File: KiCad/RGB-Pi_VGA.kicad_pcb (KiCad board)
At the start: 2 copper layers, 85 x 43.6 mm, 39 parts, among them J1 Raspberry_Pi_4, J2 SCART-F, J3 DE15_Plug_HighDensity_Mountin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, J4 SJ1-3535NG, Q1 MMBT3904, U1 ST662A

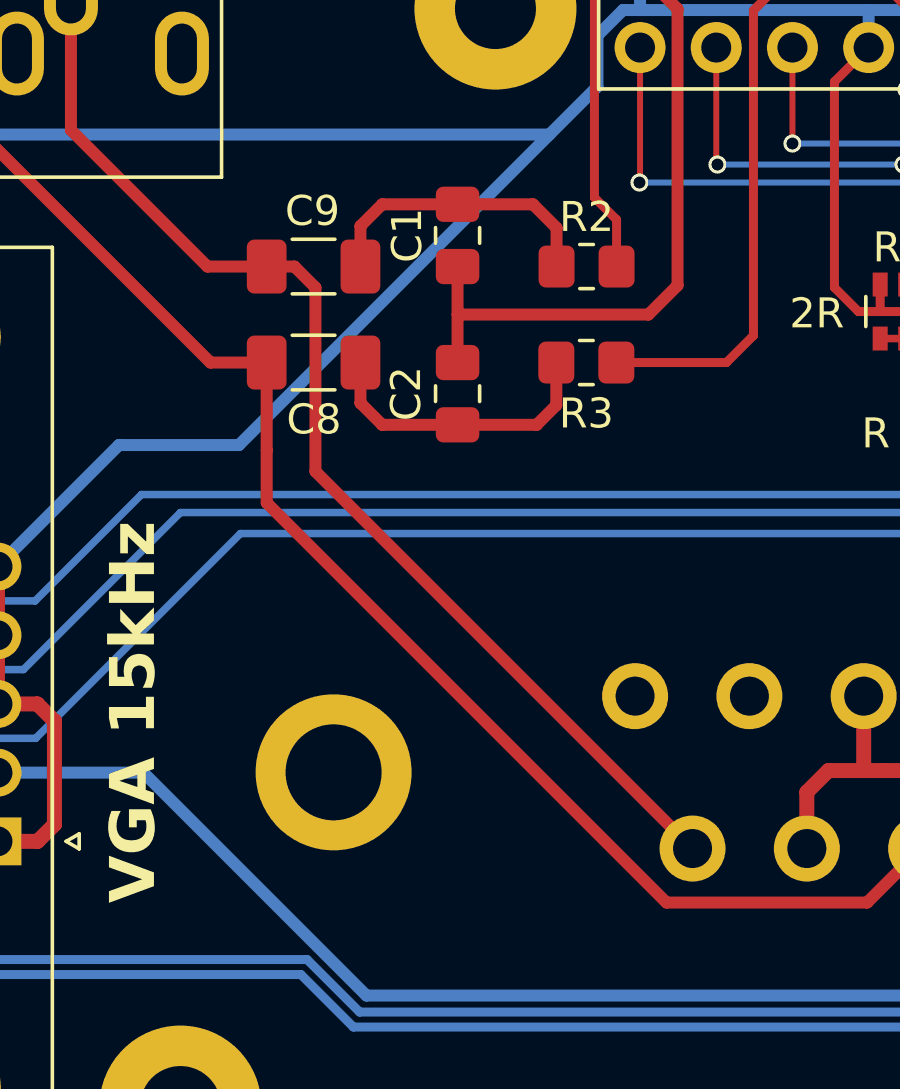
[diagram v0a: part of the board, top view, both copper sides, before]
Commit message: Change C8, C9 footprints from 1206 to 0805.
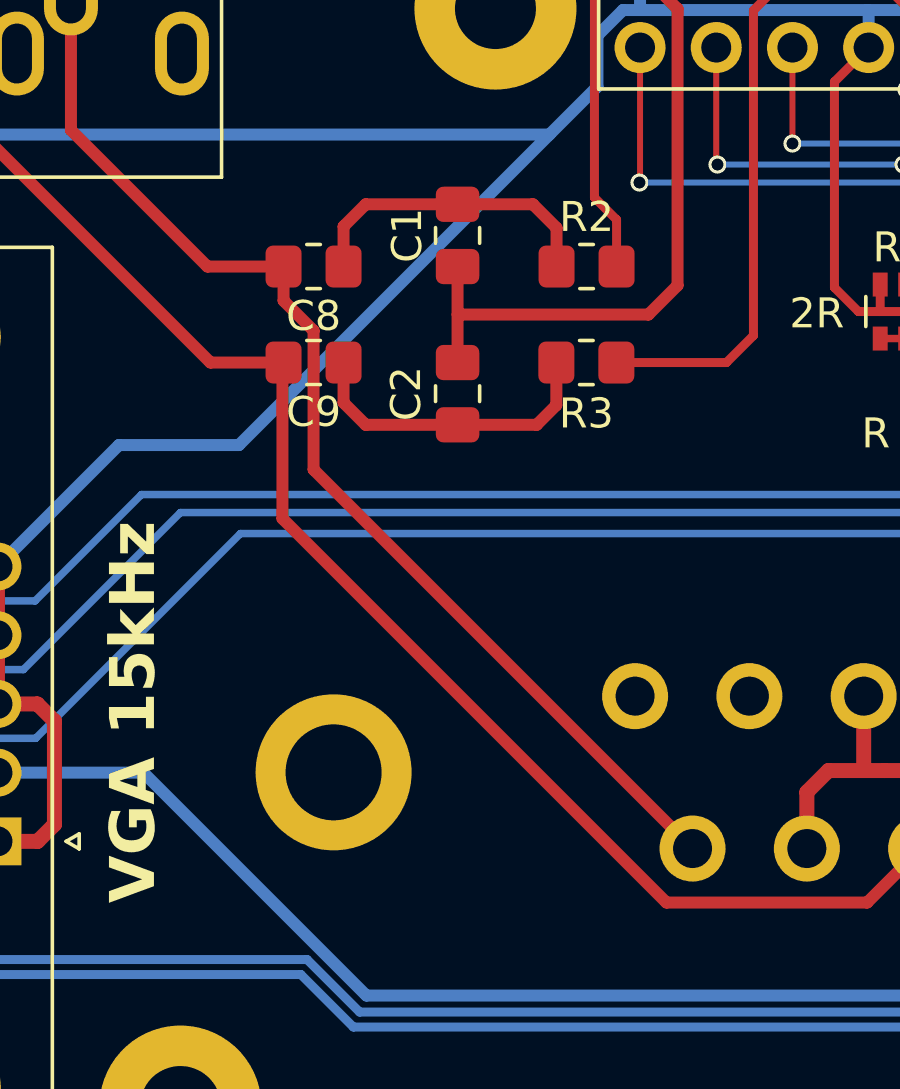
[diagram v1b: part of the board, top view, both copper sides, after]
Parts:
- C8, C9: footprint Capacitor_SMD:C_1206_3216Metric_Pad1.33x1.80mm_HandSolder -> Resistor_SMD:R_0805_2012Metric_Pad1.20x1.40mm_HandSolder
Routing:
- net Net-(C2-Pad2): track 9.87 -> 10.4 mm
- net Net-(C1-Pad2): track 9.80 -> 10.4 mm

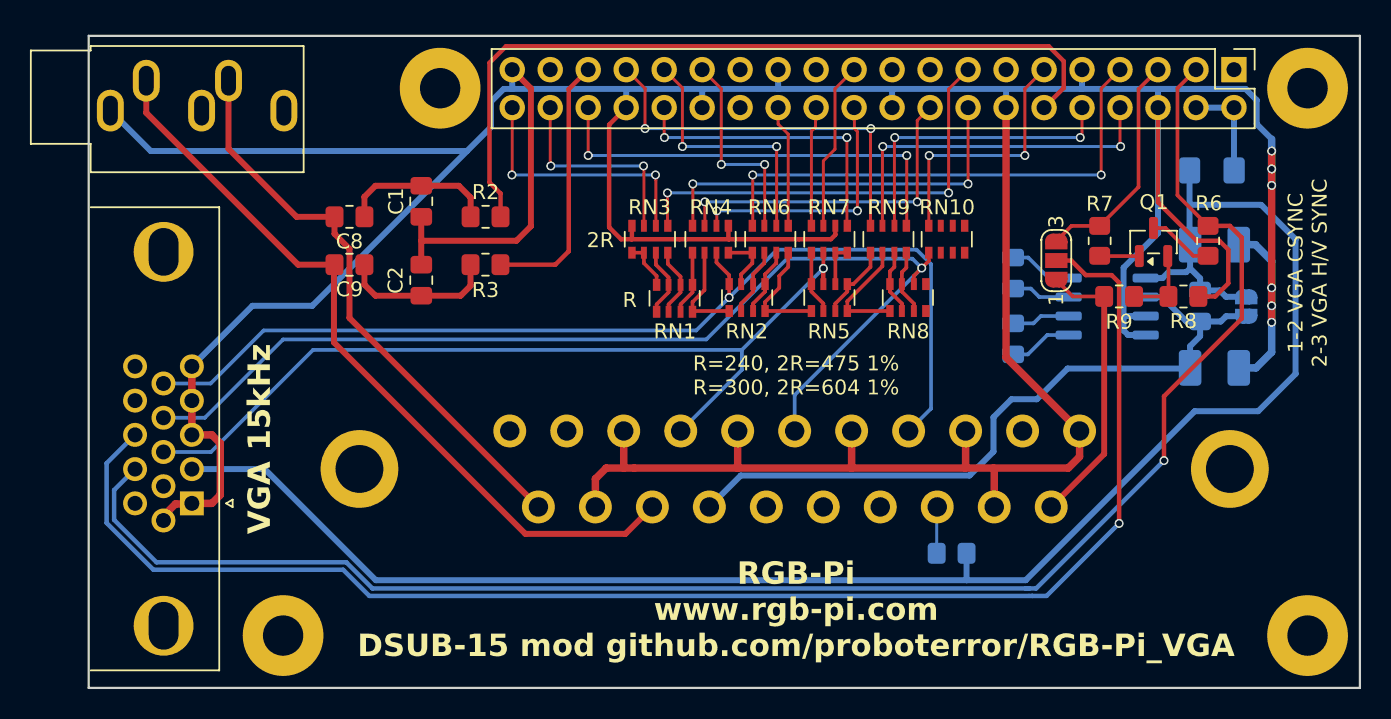
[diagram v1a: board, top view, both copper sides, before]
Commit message: Update PCB matching schematic.
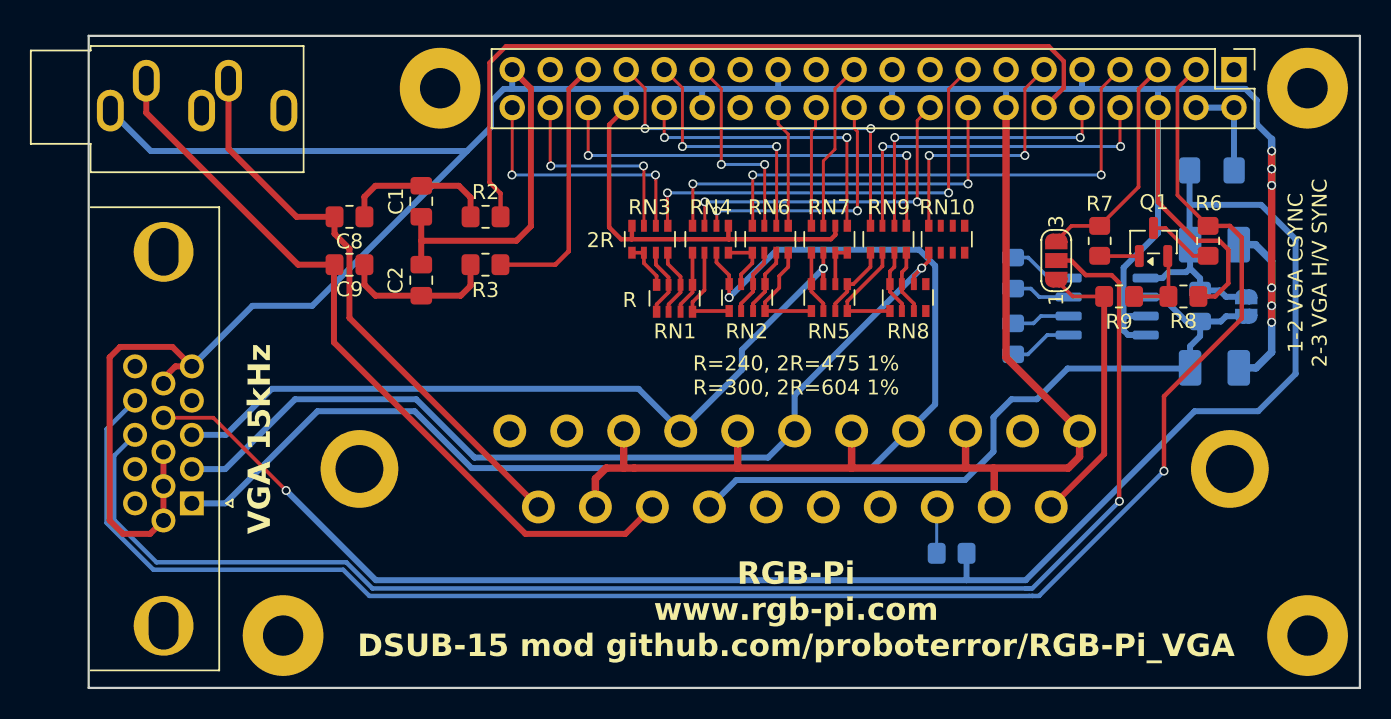
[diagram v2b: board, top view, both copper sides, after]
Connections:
- J3 pad 1: GND -> RED
- J3 pad 10: RED -> GND
- J3 pad 12: VSYNC -> unconnected-(J3-Pad12)
- J3 pad 14: unconnected-(J3-Pad14) -> VSYNC
- J3 pad 2: +5V -> GREEN
- J3 pad 3: GND -> BLUE
- J3 pad 4: GND -> unconnected-(J3-Pad4)
- J3 pad 7: unconnected-(J3-Pad7) -> GND
- J3 pad 8: BLUE -> GND
- J3 pad 9: GREEN -> +5V
- J3 pad SH: unconnected-(J3-PadSH) -> (no net)
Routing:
- net GND: track 321.7 -> 335.9 mm
- net RED: track 70.6 -> 83.8 mm
- net GREEN: track 72.3 -> 61.6 mm
- net BLUE: track 59.5 -> 53.1 mm
- net VSYNC: track 111.1 -> 117.3 mm
- net +5V: track 116.1 -> 119.4 mm, vias 0 -> 1
- net /VGA_H_SYNC: track 99.3 -> 97.2 mm

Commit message: Board version 1.1. Correct VGA connector pinout. PWM audio buffered with SN74LVC2G34 Dual Buffer Gate, powered from PS7A2033 Ultra-Low-Noise LDO, with separate analog ground, in order to reduce Raspberry Pi internal power noise. PWM output serial resistors changed from 220R to 1K. Update project description.
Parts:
- added C10: 1uF, Capacitor_SMD:C_0805_2012Metric_Pad1.18x1.45mm_HandSolder, B.Cu at (92.3, 99.0)
- added C11: 1uF, Capacitor_SMD:C_0805_2012Metric_Pad1.18x1.45mm_HandSolder, B.Cu at (84.3, 99.0)
- added R4: 0R, Resistor_SMD:R_0805_2012Metric_Pad1.20x1.40mm_HandSolder, B.Cu at (94.9, 95.1)
- added U2: SN74LVC2G34DBVR, Package_TO_SOT_SMD:SOT-23-6_Handsoldering, B.Cu at (85.7, 94.7)
- added U3: TPS7A2033PDBVR, Package_TO_SOT_SMD:SOT-23-5, B.Cu at (88.3, 98.9)
- C1, C2, C8, C9: moved to B.Cu
- R2, R3: value 220R -> 1K; moved to B.Cu
- moved R2 12.5 mm to (81.6, 94.6), turned to -90 degrees
- moved R3 12.4 mm to (81.6, 99.0), turned to 90 degrees
- moved C2 10.9 mm to (78.9, 99.0), turned to 90 degrees
- moved C1 10.7 mm to (79.0, 94.6), turned to -90 degrees
- moved C8 8.67 mm to (76.4, 94.6), turned to 90 degrees
- moved C9 8.54 mm to (76.4, 99.0), turned to -90 degrees
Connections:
- C1 pad 1: GND -> AGND
- C2 pad 1: GND -> AGND
- J4 pad S: GND -> AGND
- R2 pad 1: AUDIO_PWM_R -> Net-(R2-Pad1)
- R3 pad 1: AUDIO_PWM_L -> Net-(R3-Pad1)
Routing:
- net +5V: track 119.4 -> 201.8 mm, vias 1 -> 7
- net GND: track 335.9 -> 285.7 mm, vias 6 -> 0
- net /AUDIO_L: track 52.3 -> 66.0 mm
- net +3V3: track 0.00 -> 8.32 mm
- net Net-(R3-Pad1): track 0.00 -> 6.69 mm
- net Net-(C2-Pad2): track 10.4 -> 5.23 mm
- net Net-(C1-Pad2): track 10.4 -> 5.23 mm
- net /AUDIO_R: track 38.9 -> 43.9 mm
- net AUDIO_PWM_L: track 17.6 -> 21.4 mm, vias 0 -> 1
- net AUDIO_PWM_R: track 53.6 -> 57.3 mm, vias 0 -> 1
- net Net-(R2-Pad1): track 0.00 -> 2.74 mm
- net R1: track 17.5 -> 16.9 mm
- added copper zone on B.Cu, net AGND
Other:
- board text added: "V.1.1"
